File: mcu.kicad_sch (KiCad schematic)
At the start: 14 parts, among them J1 USB_C_Receptacle_USB2.0_16P, SW1 SW_Push, U1 ESP32-S3-MINI-1U

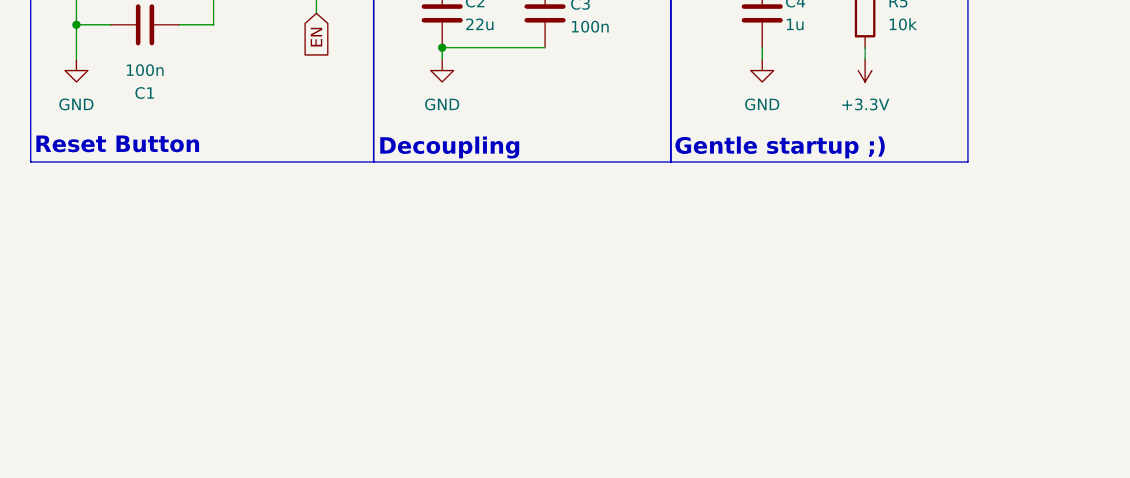
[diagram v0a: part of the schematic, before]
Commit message: MCU added  ACDC and Buck
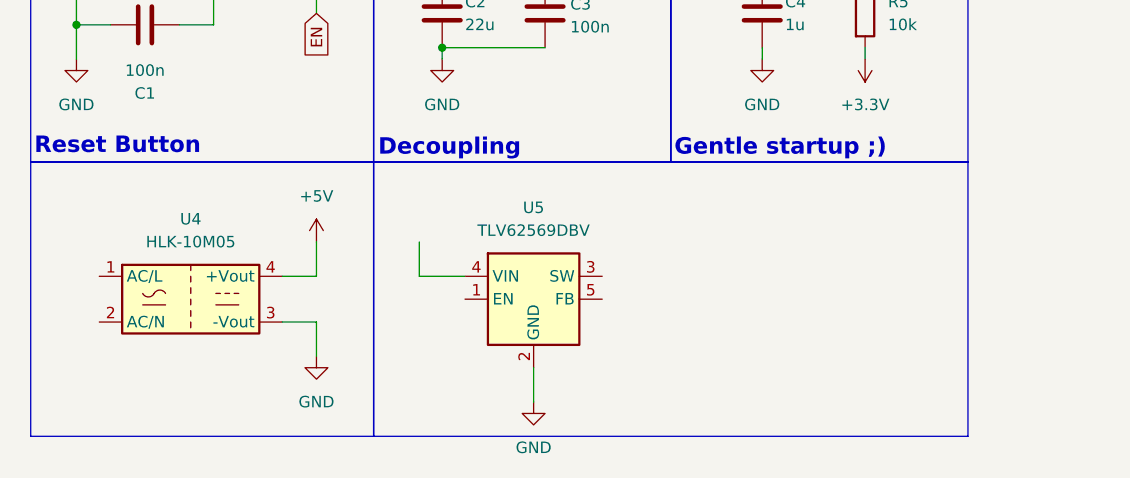
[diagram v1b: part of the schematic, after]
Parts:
- added U4: HLK-10M05, Converter_ACDC:Converter_ACDC_Hi-Link_HLK-10Mxx, symbol Converter_ACDC:HLK-10M05
- added U5: TLV62569DBV, Package_TO_SOT_SMD:SOT-23-5, symbol Regulator_Switching:TLV62569DBV
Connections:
- net +5V: now also U4.4 (+Vout)
- net GND: now also U4.3 (-Vout), U5.2 (GND)

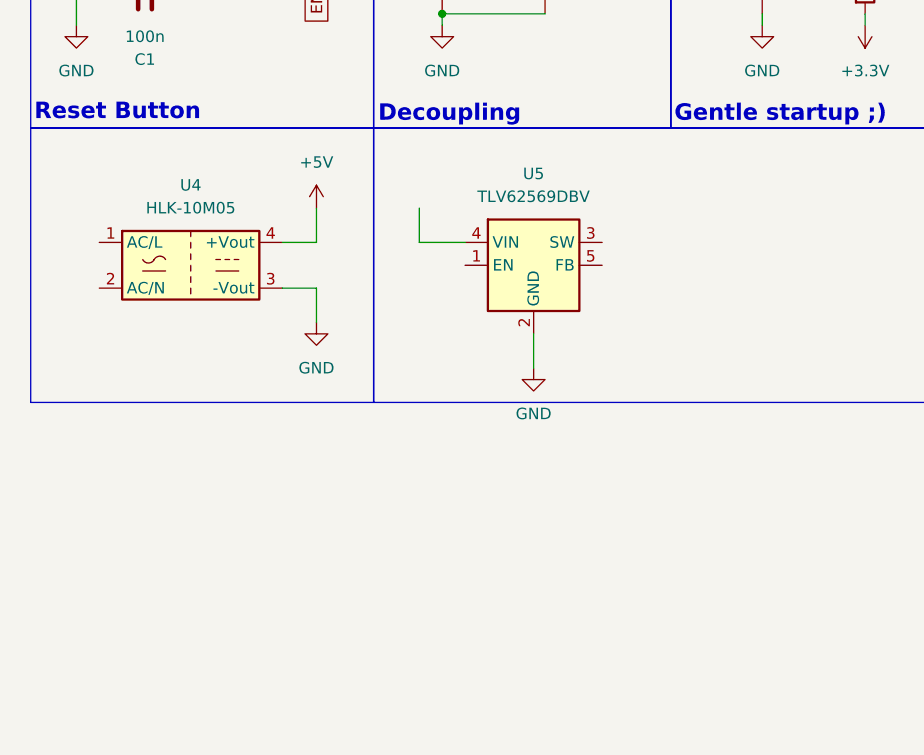
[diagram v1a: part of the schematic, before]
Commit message: Set buck passives, ADE intro
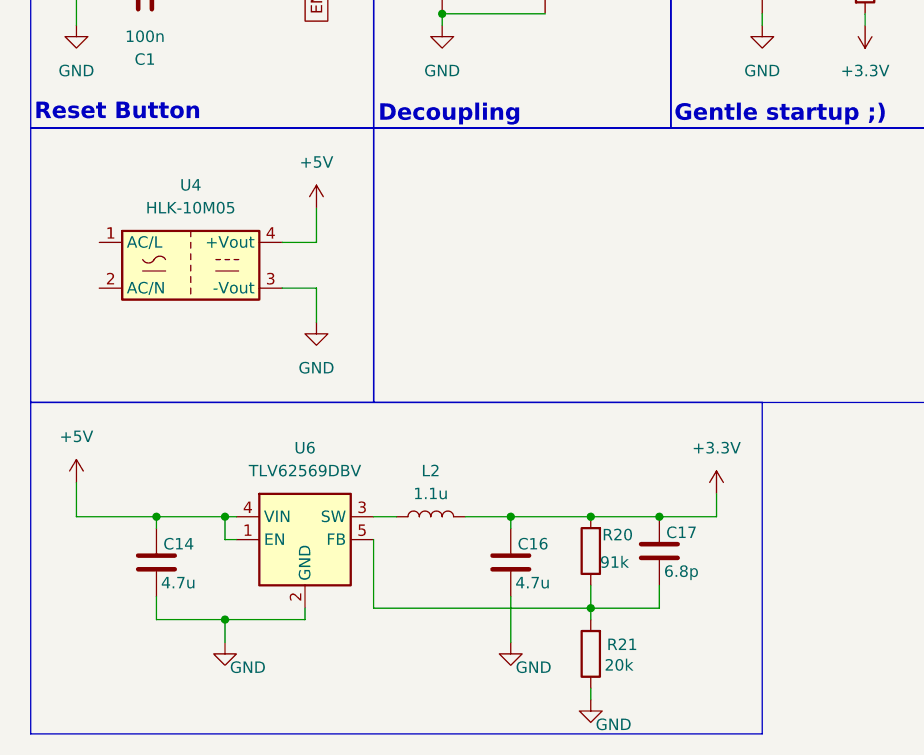
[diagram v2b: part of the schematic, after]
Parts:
- removed U5: TLV62569DBV, Package_TO_SOT_SMD:SOT-23-5, symbol Regulator_Switching:TLV62569DBV
- added C14, C16: 4.7u, symbol Device:C
- added C17: 6.8p, symbol Device:C
- added L2: 1.1u, symbol Device:L
- added R20: 91k, symbol Device:R
- added R21: 20k, symbol Device:R
- added U6: TLV62569DBV, Package_TO_SOT_SMD:SOT-23-5, symbol Regulator_Switching:TLV62569DBV
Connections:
- net +3.3V: now also C16.1, C17.1, L2.2, R20.2
- net +5V: now also C14.1, U6.1 (EN), U6.4 (VIN)
- net GND: now also C14.2, C16.2, R21.1, U6.2 (GND)
- new net: C17.2, R20.1, R21.2, U6.5 (FB)
- new net: L2.1, U6.3 (SW)

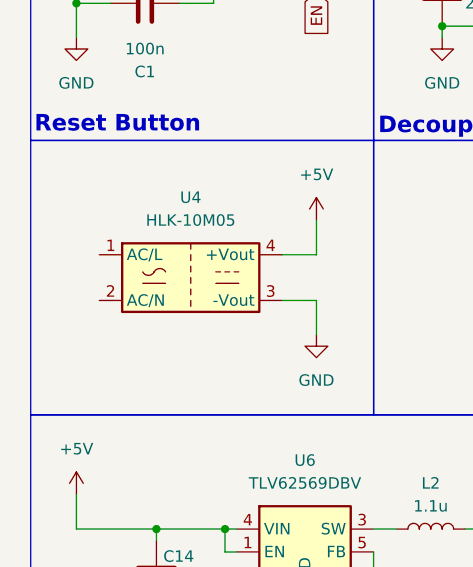
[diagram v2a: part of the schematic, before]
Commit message: added ADE periph
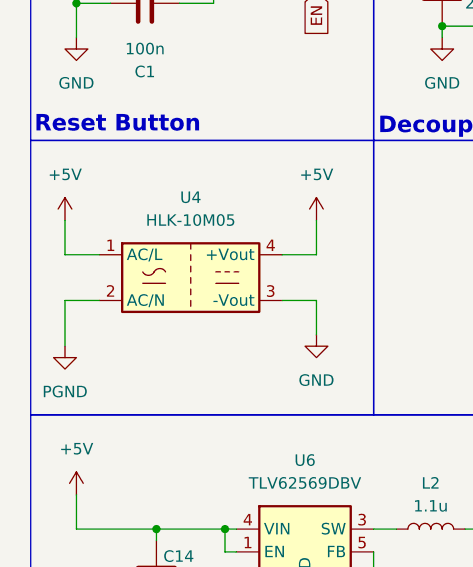
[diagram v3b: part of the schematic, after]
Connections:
- net +5V: now also U4.1 (AC/L)
- net PGND: now reaches U4.2 (AC/N)
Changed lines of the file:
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@@
 	(wire
 		(pts
+			(xy 16.51 138.43) (xy 20.32 138.43)
+		)
+		(stroke
+			(width 0)
+			(type default)
+		)
+	)
+	(wire
+		(pts
 			(xy 101.6 68.58) (xy 101.6 69.85)
 		)
@@
 	(wire
 		(pts
+			(xy 20.32 133.35) (xy 16.51 133.35)
+		)
+		(stroke
+			(width 0)
+			(type default)
+		)
+	)
+	(wire
+		(pts
 			(xy 67.31 34.29) (xy 60.96 34.29)
 		)
@@
 	(wire
 		(pts
+			(xy 16.51 133.35) (xy 16.51 129.54)
+		)
+		(stroke
+			(width 0)
+			(type default)
+		)
+	)
+	(wire
+		(pts
 			(xy 104.14 59.69) (xy 104.14 60.96)
 		)
@@
 	(wire
 		(pts
+			(xy 16.51 143.51) (xy 16.51 138.43)
+		)
+		(stroke
+			(width 0)
+			(type default)
+		)
+	)
+	(wire
+		(pts
 			(xy 82.55 171.45) (xy 82.55 173.99)
 		)
@@
 	)
 	(symbol
+		(lib_id "power:+3.3V")
+		(at 16.51 129.54 0)
+		(unit 1)
+		(body_style 1)
+		(exclude_from_sim no)
+		(in_bom yes)
+		(on_board yes)
+		(in_pos_files yes)
+		(dnp no)
+		(fields_autoplaced yes)
+		(property "Reference" "#PWR033"
+			(at 16.51 133.35 0)
+			(hide yes)
+			(show_name no)
+			(do_not_autoplace no)
+			(effects
+				(font
+					(size 1.27 1.27)
+				)
+			)
+		)
+		(property "Value" "+5V"
+			(at 16.51 124.46 0)
+			(show_name no)
+			(do_not_autoplace no)
+			(effects
+				(font
+					(size 1.27 1.27)
+				)
+			)
+		)
+		(property "Footprint" "Package_DFN_QFN:Diodes_UDFN3810-9_TYPE_B"
+			(at 16.51 129.54 0)
+			(hide yes)
+			(show_name no)
+			(do_not_autoplace no)
+			(effects
+				(font
+					(size 1.27 1.27)
+				)
+			)
+		)
+		(property "Datasheet" ""
+			(at 16.51 129.54 0)
+			(hide yes)
+			(show_name no)
+			(do_not_autoplace no)
+			(effects
+				(font
+					(size 1.27 1.27)
+				)
+			)
+		)
+		(property "Description" "Power symbol creates a global label with name \"+3.3V\""
+			(at 16.51 129.54 0)
+			(hide yes)
+			(show_name no)
+			(do_not_autoplace no)
+			(effects
+				(font
+					(size 1.27 1.27)
+				)
+			)
+		)
+		(pin "1"
+		)
+		(instances
+			(project "smart_supply"
+				(path "/487ef637-7a03-4925-80c1-798e0c6f0bbd/f9380e13-e191-4828-b42d-2cc7f479b711"
+					(reference "#PWR033")
+					(unit 1)
+				)
+			)
+		)
+	)
+	(symbol
 		(lib_id "Switch:SW_Push")
 		(at 25.4 100.33 0)
@@
 					(unit 1)
 				)
+			)
+		)
+	)
+	(symbol
+		(lib_id "power:GND")
+		(at 16.51 143.51 0)
+		(unit 1)
+		(body_style 1)
+		(exclude_from_sim no)
+		(in_bom yes)
+		(on_board yes)
+		(in_pos_files yes)
+		(dnp no)
+		(fields_autoplaced yes)
+		(property "Reference" "#PWR034"
+			(at 16.51 149.86 0)
+			(hide yes)
+			(show_name no)
+			(do_not_autoplace no)
+			(effects
+				(font
+					(size 1.27 1.27)
+				)
+			)
+		)
+		(property "Value" "PGND"
+			(at 16.51 148.59 0)
+			(show_name no)
+			(do_not_autoplace no)
+			(effects
+				(font
+					(size 1.27 1.27)
+				)
+			)
+		)
+		(property "Footprint" "RF_Module:ESP32-S3-WROOM-1"
+			(at 16.51 143.51 0)
+			(hide yes)
+			(show_name no)
+			(do_not_autoplace no)
+			(effects
+				(font
+					(size 1.27 1.27)
+				)
+			)
+		)
+		(property "Datasheet" ""
+			(at 16.51 143.51 0)
+			(hide yes)
+			(show_name no)
+			(do_not_autoplace no)
+			(effects
+				(font
+					(size 1.27 1.27)
+				)
+			)
+		)
+		(property "Description" "Power symbol creates a global label with name \"GND\" , ground"
+			(at 16.51 143.51 0)
+			(hide yes)
+			(show_name no)
+			(do_not_autoplace no)
+			(effects
+				(font
+					(size 1.27 1.27)
+				)
+			)
+		)
+		(pin "1"
+		)
+		(instances
+			(project "smart_supply"
+				(path "/487ef637-7a03-4925-80c1-798e0c6f0bbd/f9380e13-e191-4828-b42d-2cc7f479b711"
+					(reference "#PWR034")
+					(unit 1)
+				)

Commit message: TRANSFORMERS AND ADE
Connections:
- net +5V: no longer U4.1 (AC/L)
- net CS: now reaches U1.14 (IO10)
- net MOSI: now reaches U1.15 (IO11)
- net SCLK: now reaches U1.16 (IO12)
- net MISO: now reaches U1.17 (IO13)
- net IRQ: now reaches U1.18 (IO14)
- net RESET: now reaches U1.19 (IO15)
- net ZX: now reaches U1.20 (IO16)
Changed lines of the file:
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@@
+	(wire
+		(pts
+			(xy 27.94 72.39) (xy 30.48 72.39)
+		)
+		(stroke
+			(width 0)
+			(type default)
+		)
+	)
+	(wire
+		(pts
+			(xy 27.94 57.15) (xy 30.48 57.15)
+		)
+		(stroke
+			(width 0)
+			(type default)
+		)
+	)
 	(wire
 		(pts
@@
 	(wire
 		(pts
+			(xy 27.94 67.31) (xy 30.48 67.31)
+		)
+		(stroke
+			(width 0)
+			(type default)
+		)
+	)
+	(wire
+		(pts
 			(xy 17.78 163.83) (xy 35.56 163.83)
 		)
@@
 	(wire
 		(pts
+			(xy 27.94 62.23) (xy 30.48 62.23)
+		)
+		(stroke
+			(width 0)
+			(type default)
+		)
+	)
+	(wire
+		(pts
 			(xy 44.45 138.43) (xy 44.45 142.24)
 		)
@@
 	(wire
 		(pts
+			(xy 27.94 59.69) (xy 30.48 59.69)
+		)
+		(stroke
+			(width 0)
+			(type default)
+		)
+	)
+	(wire
+		(pts
 			(xy 40.64 133.35) (xy 44.45 133.35)
 		)
@@
 	(wire
 		(pts
+			(xy 27.94 64.77) (xy 30.48 64.77)
+		)
+		(stroke
+			(width 0)
+			(type default)
+		)
+	)
+	(wire
+		(pts
 			(xy 33.02 100.33) (xy 36.83 100.33)
 		)
@@
 	(wire
 		(pts
+			(xy 27.94 69.85) (xy 30.48 69.85)
+		)
+		(stroke
+			(width 0)
+			(type default)
+		)
+	)
+	(wire
+		(pts
 			(xy 60.96 163.83) (xy 66.04 163.83)
 		)
@@
 			(width 0)
 			(type default)
+		)
+	)
+	(label "IRQ"
+		(at 27.94 67.31 180)
+		(effects
+			(font
+				(size 1.27 1.27)
+			)
+			(justify right bottom)
+		)
+	)
+	(label "CS"
+		(at 27.94 57.15 180)
+		(effects
+			(font
+				(size 1.27 1.27)
+			)
+			(justify right bottom)
+		)
+	)
+	(label "SCLK"
+		(at 27.94 62.23 180)
+		(effects
+			(font
+				(size 1.27 1.27)
+			)
+			(justify right bottom)
+		)
+	)
+	(label "ZX"
+		(at 27.94 72.39 180)
+		(effects
+			(font
+				(size 1.27 1.27)
+			)
+			(justify right bottom)
+		)
+	)
+	(label "MISO"
+		(at 27.94 64.77 180)
+		(effects
+			(font
+				(size 1.27 1.27)
+			)
+			(justify right bottom)
+		)
+	)
+	(label "RESET"
+		(at 27.94 69.85 180)
+		(effects
+			(font
+				(size 1.27 1.27)
+			)
+			(justify right bottom)
+		)
+	)
+	(label "MOSI"
+		(at 27.94 59.69 180)
+		(effects
+			(font
+				(size 1.27 1.27)
+			)
+			(justify right bottom)
 		)
 	)
@@
 			)
 		)
-		(property "Value" "+5V"
+		(property "Value" ""
 			(at 16.51 124.46 0)
 			(show_name no)

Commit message: 2nd ADE
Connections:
- net CS2: now reaches U1.21 (IO17)
- net IRQ2: now reaches U1.22 (IO18)
- net CS renamed CS1
- net IRQ renamed IRQ1
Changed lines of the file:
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@@
+	(wire
+		(pts
+			(xy 27.94 77.47) (xy 30.48 77.47)
+		)
+		(stroke
+			(width 0)
+			(type default)
+		)
+	)
 	(wire
 		(pts
@@
 	(wire
 		(pts
+			(xy 27.94 74.93) (xy 30.48 74.93)
+		)
+		(stroke
+			(width 0)
+			(type default)
+		)
+	)
+	(wire
+		(pts
 			(xy 60.96 29.21) (xy 67.31 29.21)
 		)
@@
 		)
 	)
-	(label "IRQ"
+	(label "IRQ1"
 		(at 27.94 67.31 180)
 		(effects
@@
 		)
 	)
-	(label "CS"
+	(label "CS2"
+		(at 27.94 74.93 180)
+		(effects
+			(font
+				(size 1.27 1.27)
+			)
+			(justify right bottom)
+		)
+	)
+	(label "CS1"
 		(at 27.94 57.15 180)
 		(effects
@@
 		(effects
 			(font
+				(size 1.27 1.27)
+			)
+			(justify right bottom)
+		)
+	)
+	(label "IRQ2"
+		(at 27.94 77.47 180)
+		(effects
+			(font

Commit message: relay connections
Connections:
- net L: now reaches U4.1 (AC/L)
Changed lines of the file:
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@@
-	)
-	(symbol
-		(lib_id "power:+3.3V")
-		(at 16.51 129.54 0)
-		(unit 1)
-		(body_style 1)
-		(exclude_from_sim no)
-		(in_bom yes)
-		(on_board yes)
-		(in_pos_files yes)
-		(dnp no)
-		(fields_autoplaced yes)
-		(property "Reference" "#PWR033"
-			(at 16.51 133.35 0)
-			(hide yes)
-			(show_name no)
-			(do_not_autoplace no)
-			(effects
-				(font
-					(size 1.27 1.27)
-				)
-			)
-		)
-		(property "Value" ""
-			(at 16.51 124.46 0)
-			(show_name no)
-			(do_not_autoplace no)
-			(effects
-				(font
-					(size 1.27 1.27)
-				)
-			)
-		)
-		(property "Footprint" "Package_DFN_QFN:Diodes_UDFN3810-9_TYPE_B"
-			(at 16.51 129.54 0)
-			(hide yes)
-			(show_name no)
-			(do_not_autoplace no)
-			(effects
-				(font
-					(size 1.27 1.27)
-				)
-			)
-		)
-		(property "Datasheet" ""
-			(at 16.51 129.54 0)
-			(hide yes)
-			(show_name no)
-			(do_not_autoplace no)
-			(effects
-				(font
-					(size 1.27 1.27)
-				)
-			)
-		)
-		(property "Description" "Power symbol creates a global label with name \"+3.3V\""
-			(at 16.51 129.54 0)
-			(hide yes)
-			(show_name no)
-			(do_not_autoplace no)
-			(effects
-				(font
-					(size 1.27 1.27)
-				)
-			)
-		)
-		(pin "1"
-		)
-		(instances
-			(project "smart_supply"
-				(path "/487ef637-7a03-4925-80c1-798e0c6f0bbd/f9380e13-e191-4828-b42d-2cc7f479b711"
-					(reference "#PWR033")
-					(unit 1)
-				)
-			)
-		)
 	)
 	(symbol
@@
 	)
 	(symbol
+		(lib_id "power:+3.3V")
+		(at 16.51 129.54 0)
+		(unit 1)
+		(body_style 1)
+		(exclude_from_sim no)
+		(in_bom yes)
+		(on_board yes)
+		(in_pos_files yes)
+		(dnp no)
+		(fields_autoplaced yes)
+		(property "Reference" "#PWR049"
+			(at 16.51 133.35 0)
+			(hide yes)
+			(show_name no)
+			(do_not_autoplace no)
+			(effects
+				(font
+					(size 1.27 1.27)
+				)
+			)
+		)
+		(property "Value" "L"
+			(at 16.51 124.46 0)
+			(show_name no)
+			(do_not_autoplace no)
+			(effects
+				(font
+					(size 1.27 1.27)
+				)
+			)
+		)
+		(property "Footprint" "Package_DFN_QFN:Diodes_UDFN3810-9_TYPE_B"
+			(at 16.51 129.54 0)
+			(hide yes)
+			(show_name no)
+			(do_not_autoplace no)
+			(effects
+				(font
+					(size 1.27 1.27)
+				)
+			)
+		)
+		(property "Datasheet" ""
+			(at 16.51 129.54 0)
+			(hide yes)
+			(show_name no)
+			(do_not_autoplace no)
+			(effects
+				(font
+					(size 1.27 1.27)
+				)
+			)
+		)
+		(property "Description" "Power symbol creates a global label with name \"+3.3V\""
+			(at 16.51 129.54 0)
+			(hide yes)
+			(show_name no)
+			(do_not_autoplace no)
+			(effects
+				(font
+					(size 1.27 1.27)
+				)
+			)
+		)
+		(pin "1"
+		)
+		(instances
+			(project "smart_supply"
+				(path "/487ef637-7a03-4925-80c1-798e0c6f0bbd/f9380e13-e191-4828-b42d-2cc7f479b711"
+					(reference "#PWR049")
+					(unit 1)
+				)
+			)
+		)
+	)
+	(symbol
 		(lib_id "Converter_ACDC:HLK-10M05")
 		(at 30.48 135.89 0)
@@
 		(in_pos_files yes)
 		(dnp no)
-		(fields_autoplaced yes)
 		(property "Reference" "#PWR034"
 			(at 16.51 149.86 0)
@@
 		)
 		(property "Value" "PGND"
-			(at 16.51 148.59 0)
-			(show_name no)
-			(do_not_autoplace no)
+			(at 16.51 147.574 0)
+			(show_name no)
+			(do_not_autoplace no)

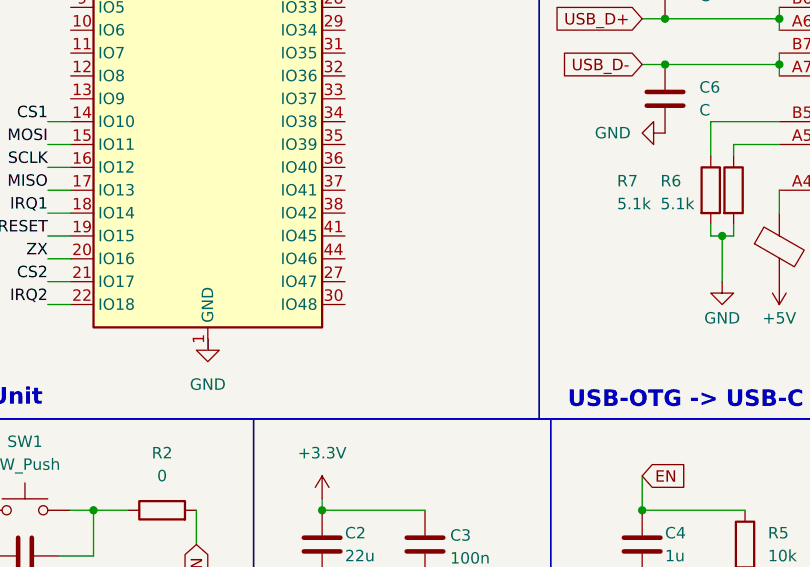
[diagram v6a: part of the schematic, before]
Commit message: POWER LINE SHEET DRAFT FINISHED
Added CH2 transformer, fuses and connectors. Foorprints TBD. Relay modules finished and assigned to MCU. VSNS and CSNS connected to lines.
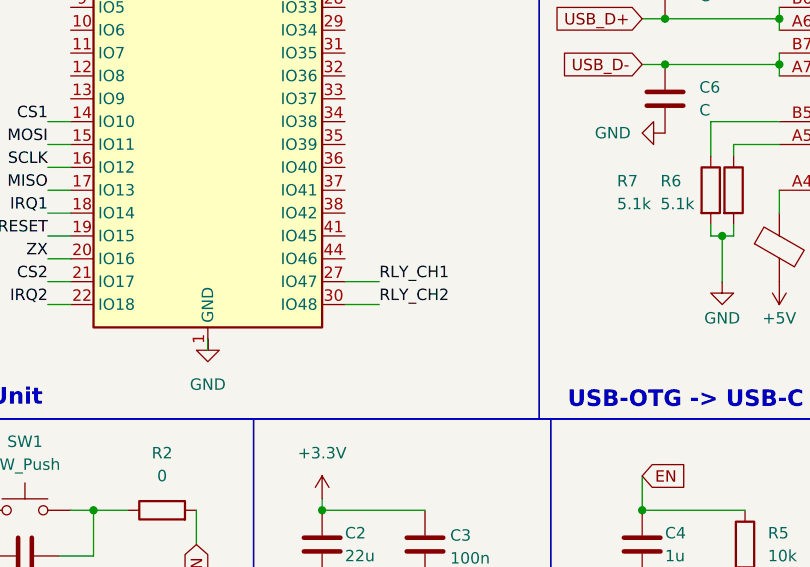
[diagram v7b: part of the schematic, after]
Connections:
- net RLY_CH1: now reaches U1.27 (IO47)
- net RLY_CH2: now reaches U1.30 (IO48)
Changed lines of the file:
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@@
+	(wire
+		(pts
+			(xy 60.96 77.47) (xy 64.77 77.47)
+		)
+		(stroke
+			(width 0)
+			(type default)
+		)
+	)
 	(wire
 		(pts
@@
 		(pts
 			(xy 66.04 163.83) (xy 74.93 163.83)
+		)
+		(stroke
+			(width 0)
+			(type default)
+		)
+	)
+	(wire
+		(pts
+			(xy 60.96 74.93) (xy 64.77 74.93)
 		)
 		(stroke
@@
 		)
 	)
+	(label "RLY_CH2"
+		(at 64.77 77.47 0)
+		(effects
+			(font
+				(size 1.27 1.27)
+			)
+			(justify left bottom)
+		)
+	)
+	(label "RLY_CH1"
+		(at 64.77 74.93 0)
+		(effects
+			(font
+				(size 1.27 1.27)
+			)
+			(justify left bottom)
+		)
+	)
